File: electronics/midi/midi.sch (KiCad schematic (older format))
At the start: 7 parts

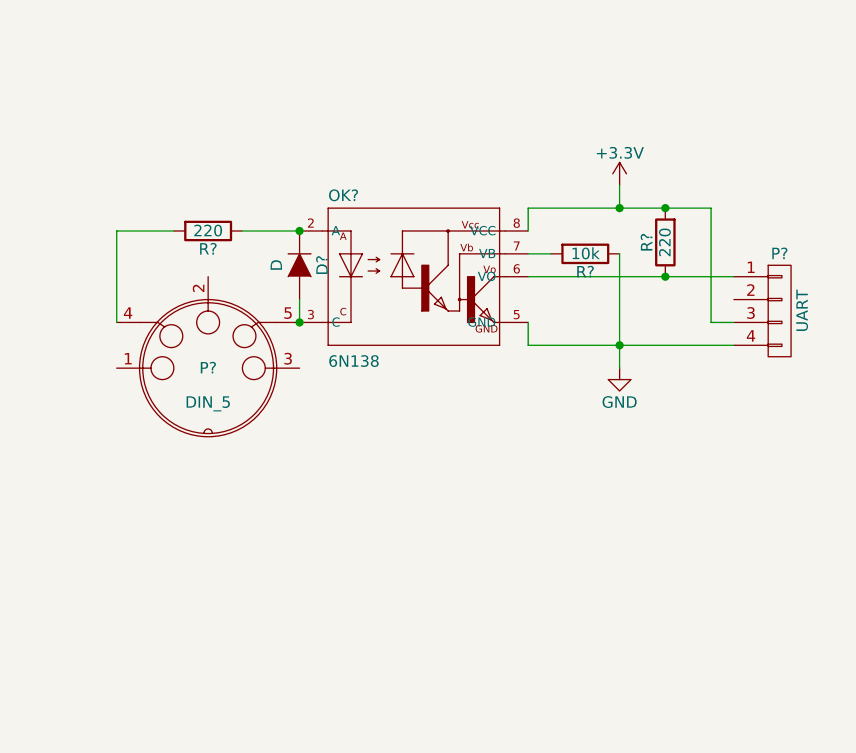
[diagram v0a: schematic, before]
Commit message: Layout MIDI_IN board
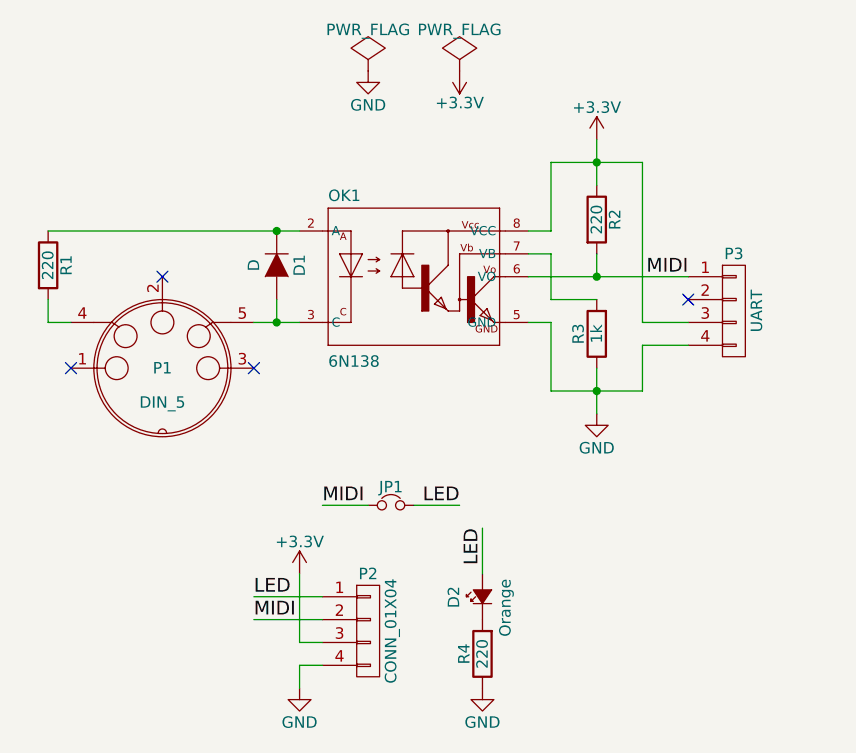
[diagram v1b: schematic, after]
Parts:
- added D2: Orange, LEDs:LED-0603, symbol Led_Small
- added JP1: Jumper_NC_Small, symbol Jumper_NC_Small
- added P2: CONN_01X04, Pin_Headers:Pin_Header_Straight_1x04, symbol CONN_01X04
- added R4: 220, Resistors_SMD:R_0603_HandSoldering, symbol R
- D1: renamed from D?; footprint (none) -> Diodes_SMD:SOD-123
- OK1: renamed from OK?; footprint optocoupler-2-DIL08 -> SMD_Packages:DIP-8_SMD
- P1: renamed from P?; footprint (none) -> Connect:SDS-50J
- P3: renamed from P?; footprint (none) -> Connectors_JST_SH:Connectors_JST_BM04B-SRSS-TB
- R1, R2: renamed from R?; footprint (none) -> Resistors_SMD:R_0603_HandSoldering
- R3: renamed from R?; value 10k -> 1k; footprint (none) -> Resistors_SMD:R_0603_HandSoldering
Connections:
- net +3V3: now also R2.1, P2.3 (P3); no longer R2.2
- net GND: now also P2.4 (P4), R4.1
- net MIDI: now reaches OK1.6 (VO), P3.1 (P1)
- net MIDI: now also R2.2, JP1.1, P2.2 (P2); no longer R2.1
- new net: D2.1 (K), R4.2
- new net LED: D2.2 (A), JP1.2, P2.1 (P1)
- no-connect marks 0 -> 4
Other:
- moved on the sheet: D1, P1, P3, R1, R2, R3

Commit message: Start updating MIDI_IN board
- add decoupling cap
- change LED polarity
- change 4-pin header to 3-pin
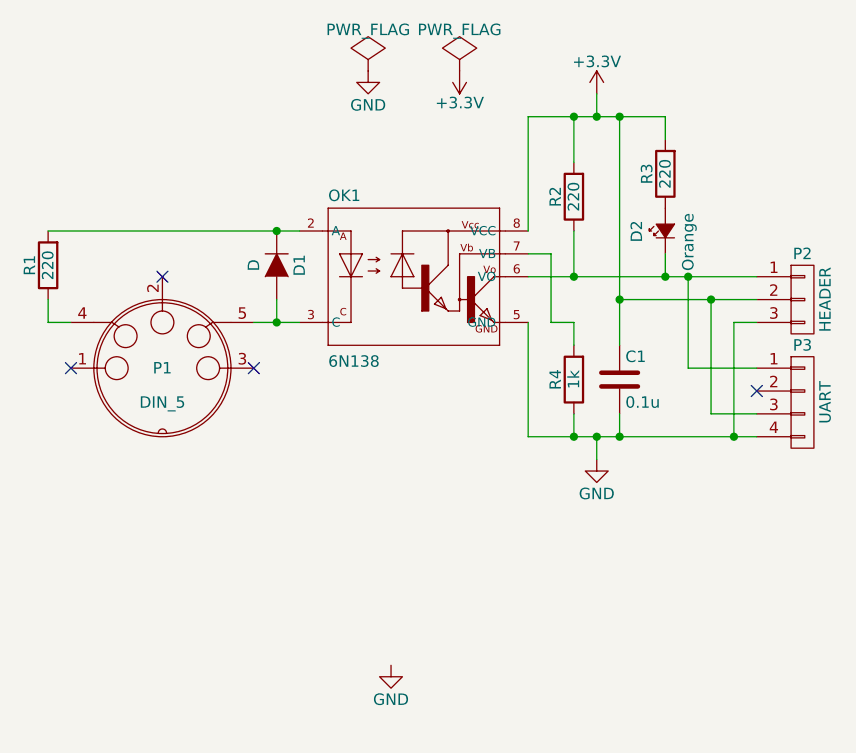
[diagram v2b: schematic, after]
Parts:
- removed JP1: Jumper_NC_Small, symbol Jumper_NC_Small
- removed P2: CONN_01X04, Pin_Headers:Pin_Header_Straight_1x04, symbol CONN_01X04
- added C1: 0.1u, Capacitors_SMD:C_0603, symbol C
- added P2: HEADER, Pin_Headers:Pin_Header_Straight_1x03, symbol CONN_01X03
- R1, R2: footprint Resistors_SMD:R_0603_HandSoldering -> Resistors_SMD:R_0603
- R3: renamed from R4; footprint Resistors_SMD:R_0603_HandSoldering -> Resistors_SMD:R_0603
- R4: renamed from R3; footprint Resistors_SMD:R_0603_HandSoldering -> Resistors_SMD:R_0603
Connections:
- net +3V3: now also R2.2, R3.2, C1.1, P2.2 (P2); no longer R2.1
- net GND: now also C1.2, P2.3 (P3); no longer R3.1
- net at D1.1 (K), OK1.2 (A): now also R1.2; no longer R1.1
- net at P1.4: now also R1.1; no longer R1.2
- net at D2.1 (K): now also OK1.6 (VO), P3.1 (P1), R2.1, P2.1 (P1); no longer R3.2
- net LED: no longer names the net of D2.2 (A)
- net LED: now also R3.1
- removed net MIDI: OK1.6 (VO), P3.1 (P1), R2.2
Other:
- moved on the sheet: D2, P3, R2, R3, R4
